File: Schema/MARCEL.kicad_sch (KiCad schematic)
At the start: 10 parts, among them SW1 Power switch

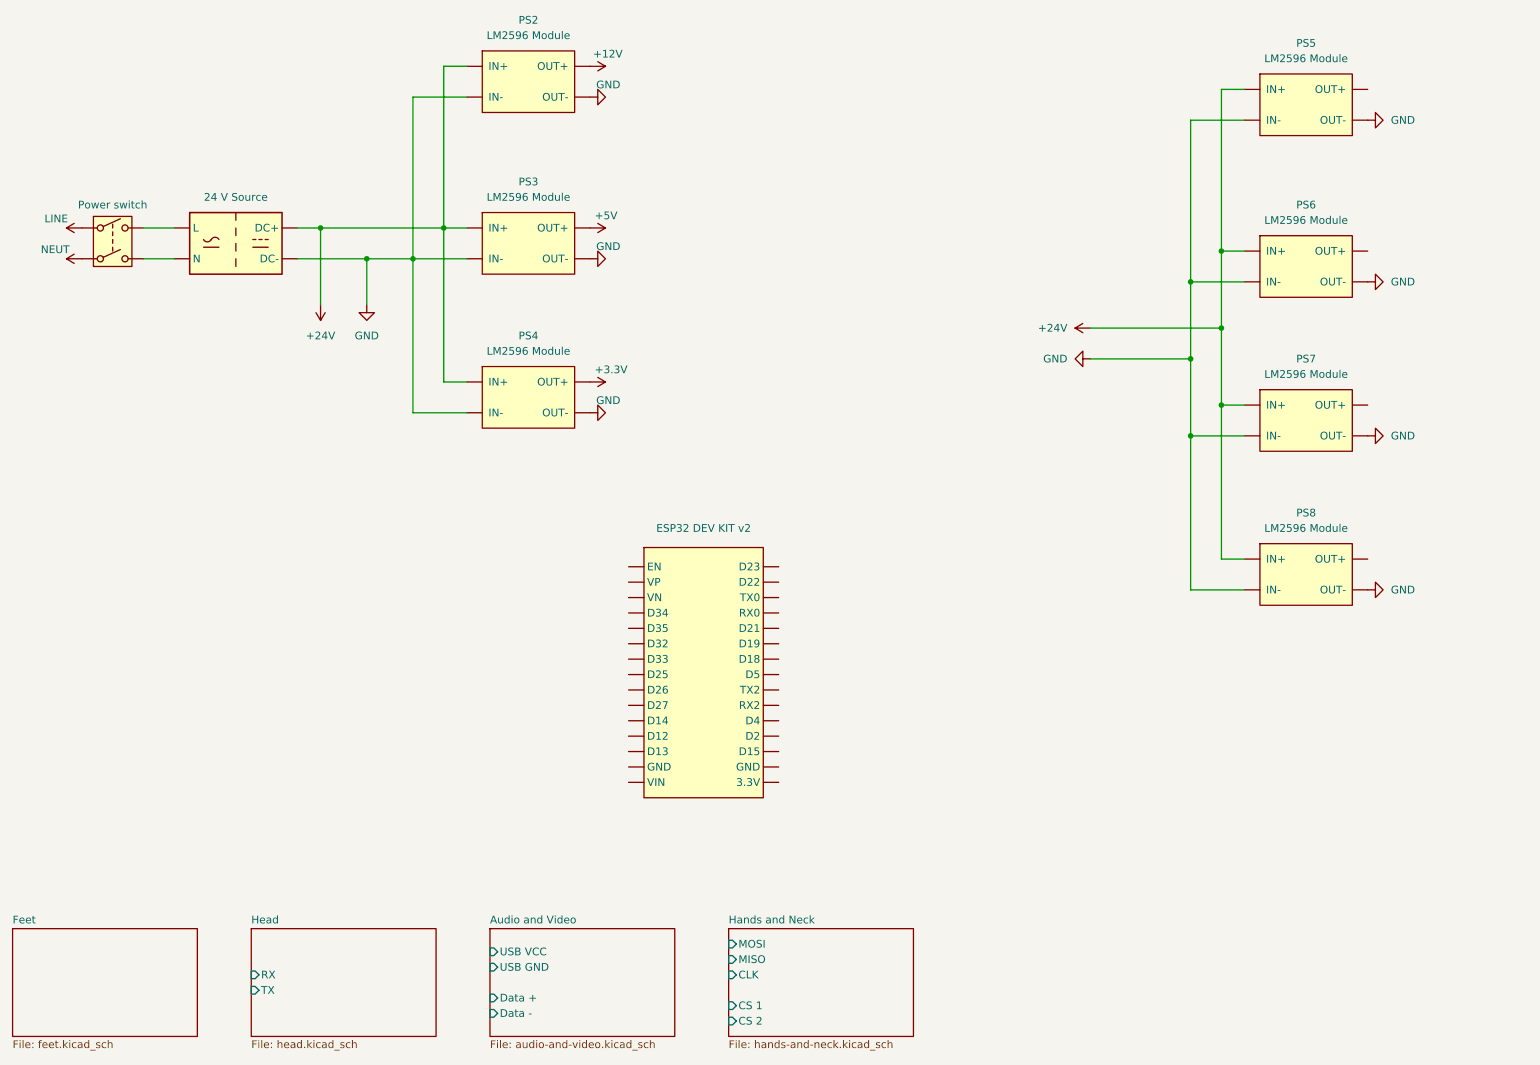
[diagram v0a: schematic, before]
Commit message: Updated schema and added math before ONCS
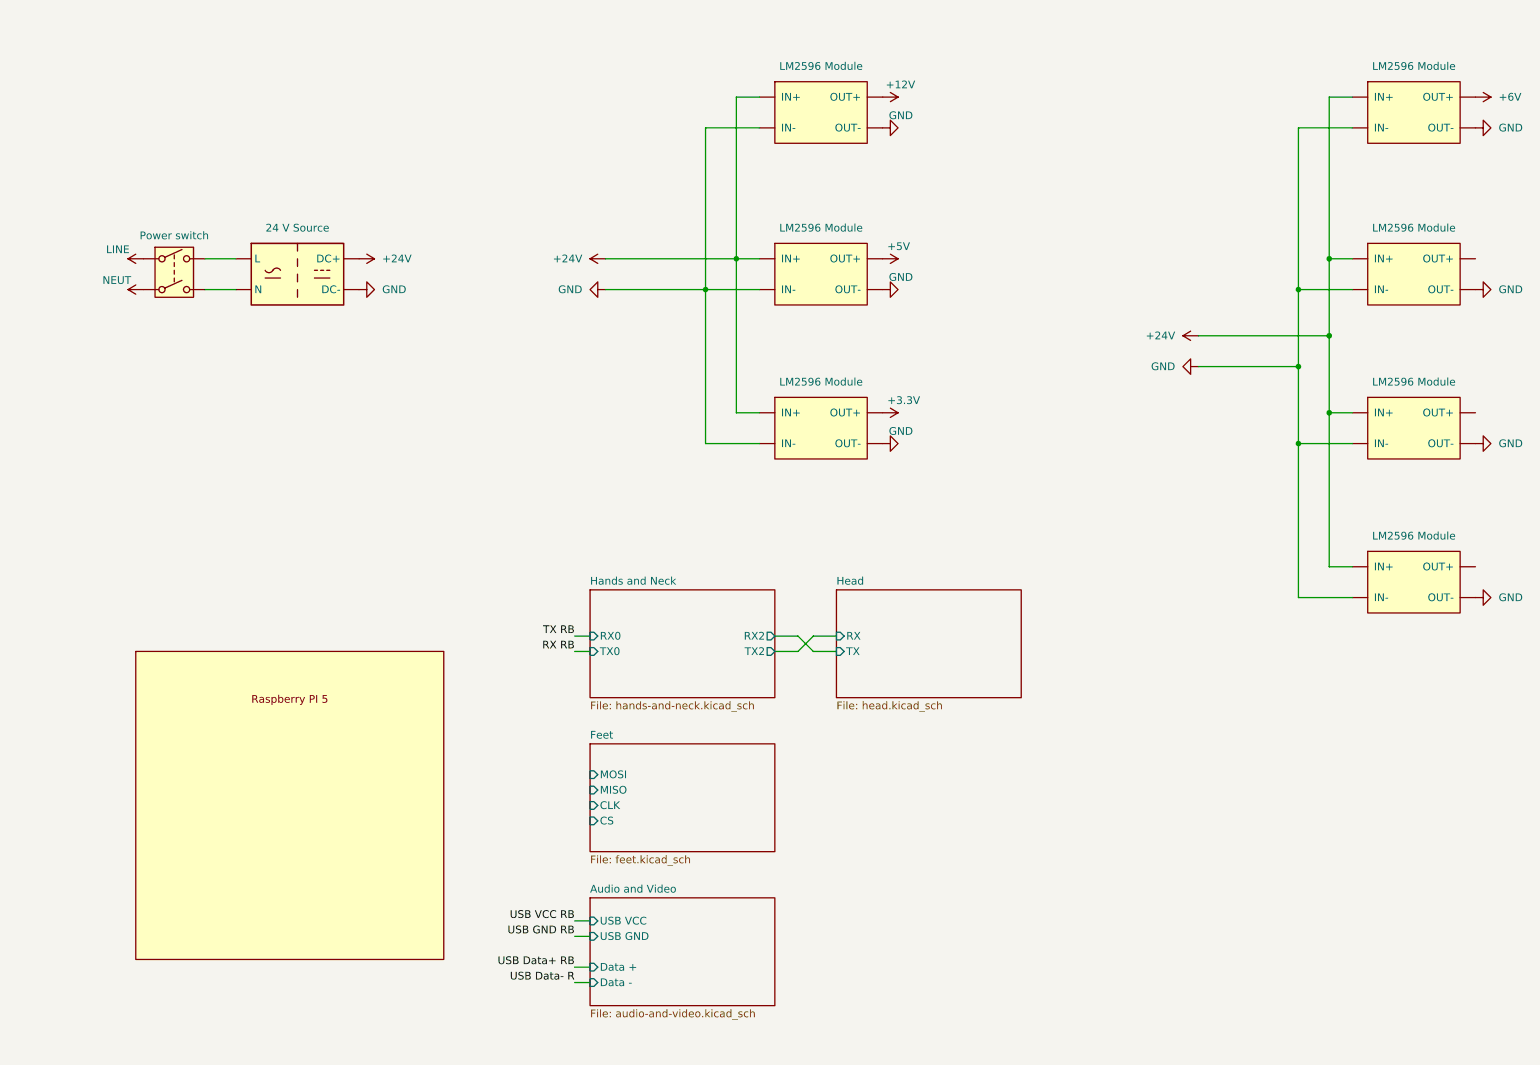
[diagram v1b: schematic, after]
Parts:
- removed ESP32 DEV KIT v2: ~, symbol MARCEL-custom:ESP32
- added U10: ~, symbol MARCEL-custom:Raspberry_PI_5
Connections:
- net +6V: now reaches PS5.3 (OUT+)
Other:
- sheet Feet ports: added CLK, CS, MISO, MOSI; removed none
- sheet Hands and Neck ports: added RX0, RX2, TX0, TX2; removed CLK, CS 1, CS 2, MISO, MOSI
